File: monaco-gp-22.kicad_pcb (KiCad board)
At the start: 2 copper layers, 101 x 48.4 mm, 2 parts

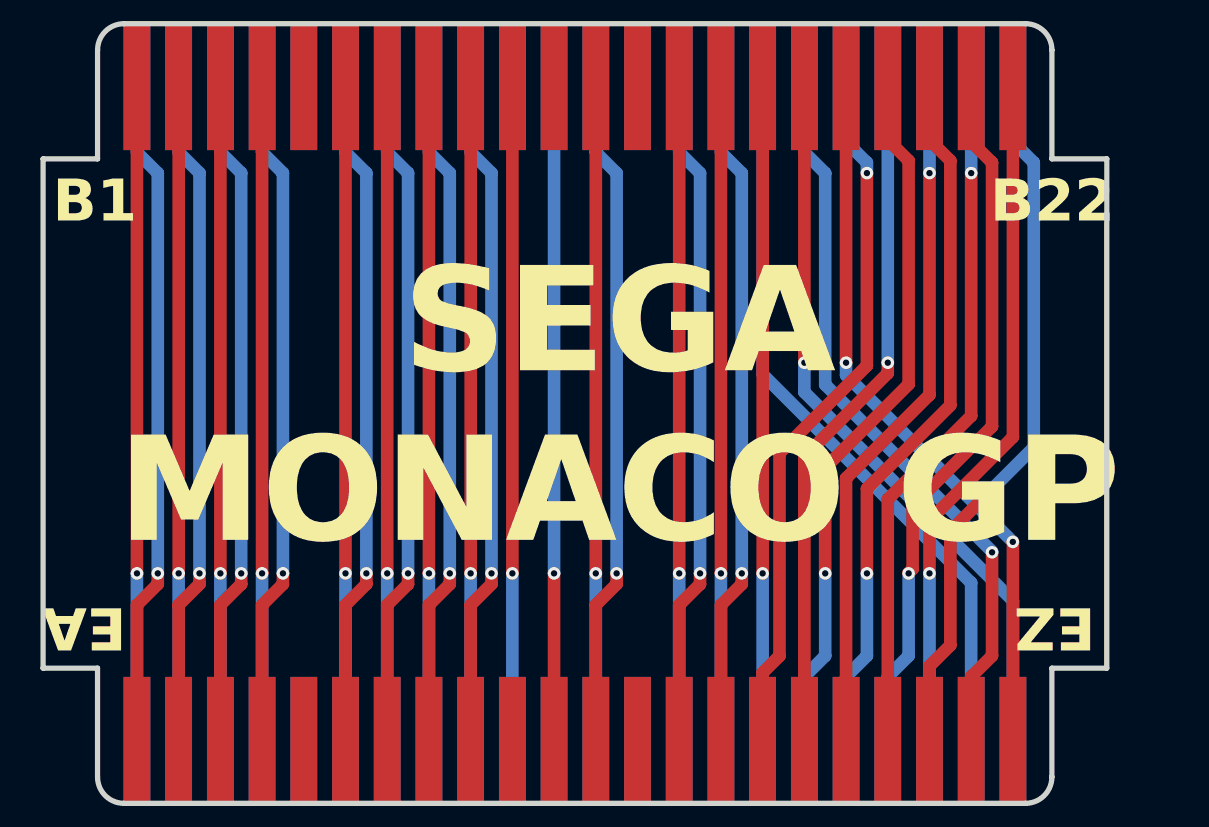
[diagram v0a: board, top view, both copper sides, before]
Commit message: cleanup, add holes, shrink connector size
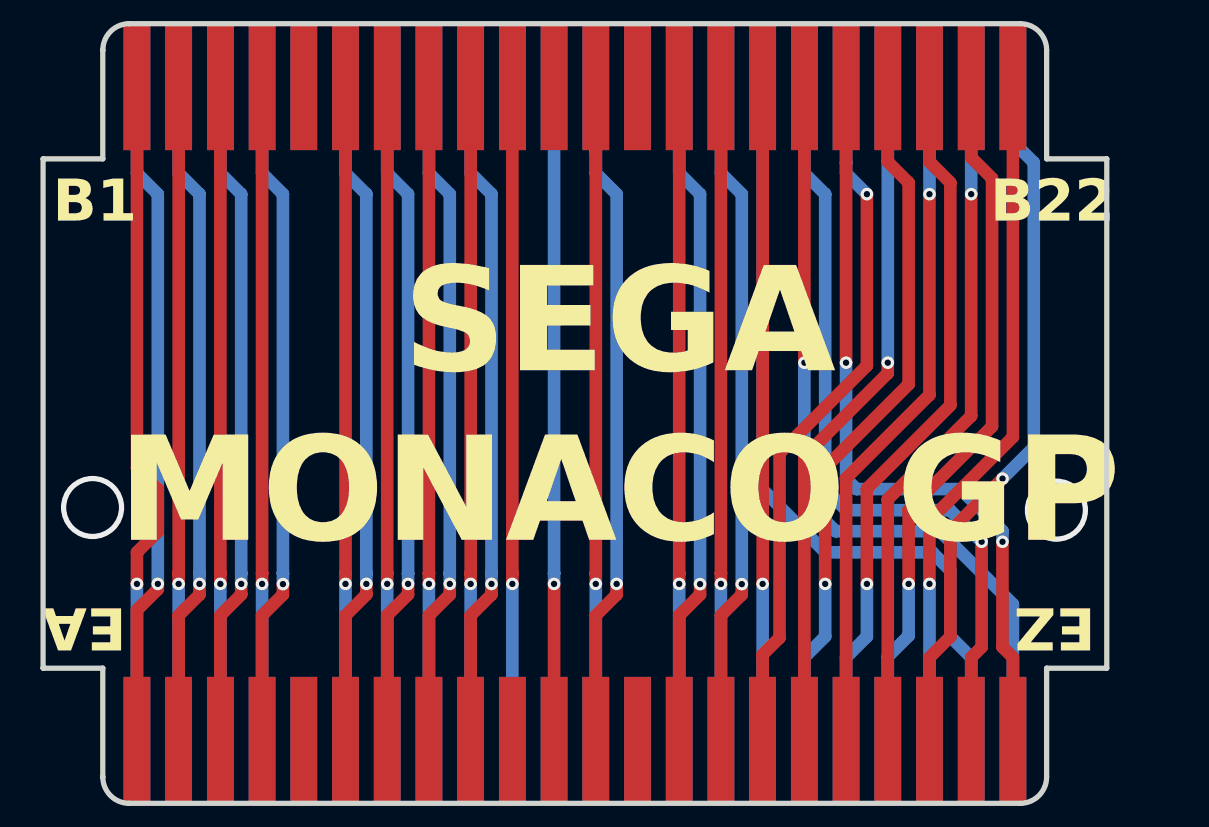
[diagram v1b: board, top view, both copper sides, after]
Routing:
- net /X21: track 70.2 -> 76.2 mm
- net /X22: track 70.2 -> 76.0 mm
- net /X44: track 68.6 -> 74.4 mm
- net /X43: track 70.2 -> 75.2 mm
- net /X1: track 62.0 -> 63.7 mm
- net (no net): vias 0 -> 2
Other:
- outline, holes or cut-outs redrawn
